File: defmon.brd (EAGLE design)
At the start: 50.8 x 48.1 mm, 18 parts, among them IC2 MEGA8-P, Q1 20MHz, X1 MAB5SH, X2 1503_09

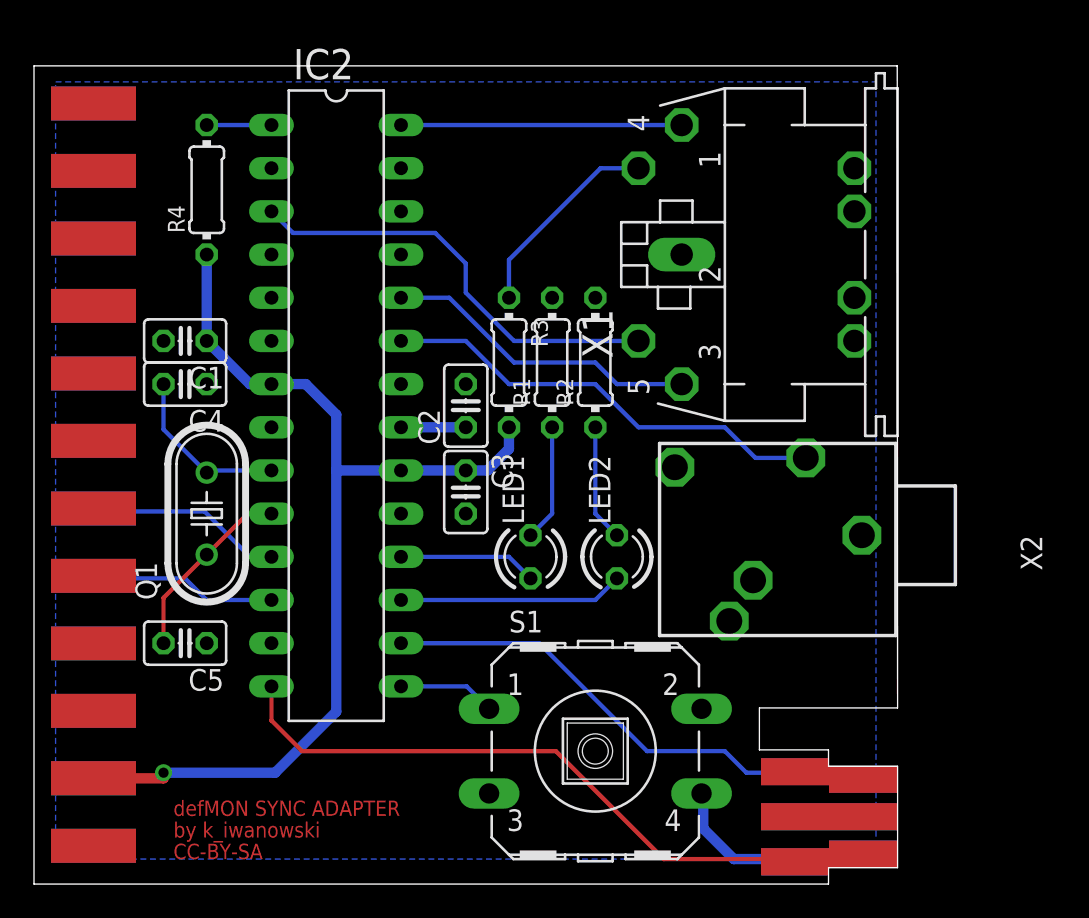
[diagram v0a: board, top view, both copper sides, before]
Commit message: added a new jack socket
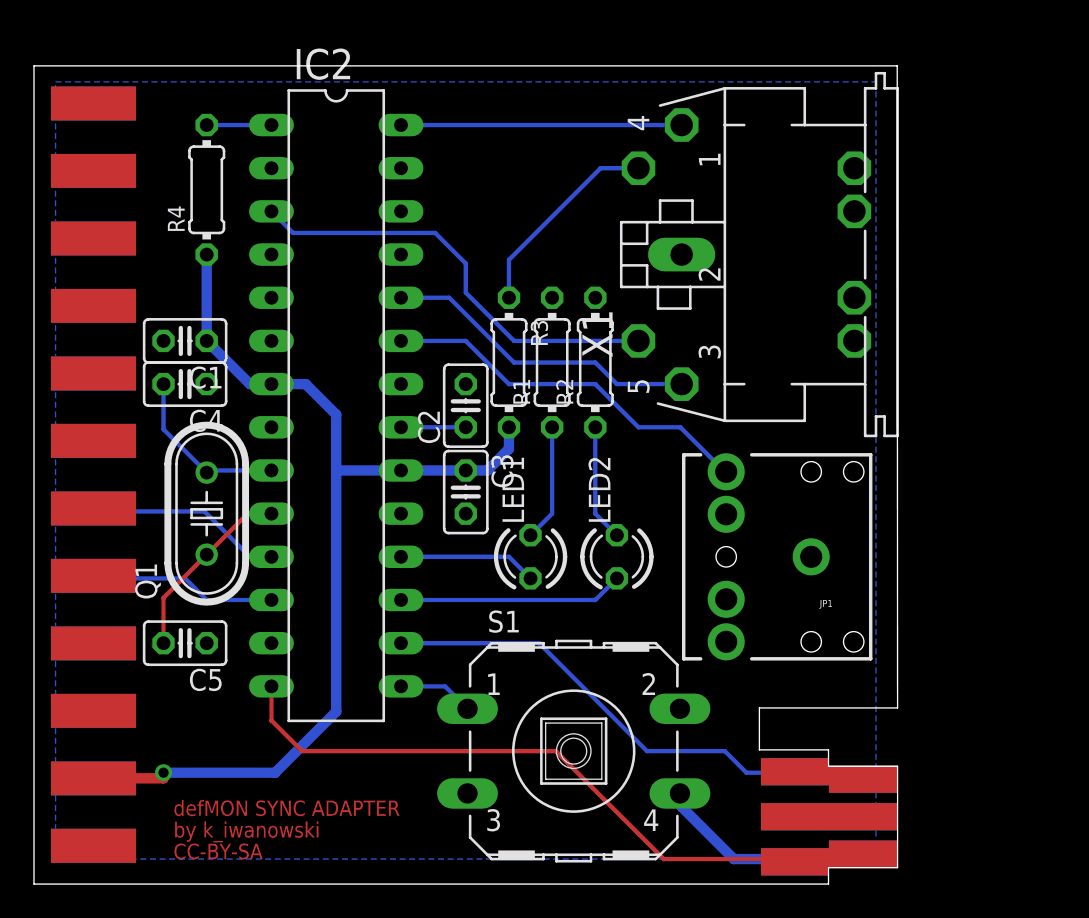
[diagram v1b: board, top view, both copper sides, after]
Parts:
- removed X2: 1503_09, con-lumberg:1503_09
- added JP1: (no value), SparkFun-Connectors:AUDIO-JACK
- moved S1 1.27 mm to (31.8, 7.62)
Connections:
- net GND: now also JP1.SLEEVE; no longer X2.1
- net TRIG1: now also JP1.TIP; no longer X2.2
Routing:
- net TRIG1: track 26.7 -> 22.3 mm
- net N$4: track 5.73 -> 4.46 mm
- net GND: track 12.6 -> 13.1 mm
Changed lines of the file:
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@@
 <layer number="54" name="bGND_GNDA" color="1" fill="9" visible="no" active="no"/>
 <layer number="56" name="wert" color="7" fill="1" visible="no" active="no"/>
+<layer number="57" name="tCAD" color="7" fill="1" visible="no" active="no"/>
+<layer number="90" name="Modules" color="5" fill="1" visible="yes" active="yes"/>
 <layer number="91" name="Nets" color="2" fill="1" visible="no" active="no"/>
 <layer number="92" name="Busses" color="1" fill="1" visible="no" active="no"/>
@@
 <layer number="97" name="Info" color="7" fill="1" visible="no" active="no"/>
 <layer number="98" name="Guide" color="6" fill="1" visible="no" active="no"/>
+<layer number="99" name="SpiceOrder" color="7" fill="1" visible="no" active="no"/>
 <layer number="100" name="Muster" color="7" fill="1" visible="no" active="no"/>
 <layer number="101" name="Patch_Top" color="12" fill="4" visible="no" active="yes"/>
@@
 <layer number="106" name="bPlate" color="7" fill="1" visible="no" active="yes"/>
 <layer number="107" name="Crop" color="7" fill="1" visible="no" active="yes"/>
+<layer number="108" name="tplace-old" color="10" fill="1" visible="yes" active="yes"/>
+<layer number="109" name="ref-old" color="11" fill="1" visible="yes" active="yes"/>
+<layer number="110" name="fp0" color="7" fill="1" visible="yes" active="yes"/>
+<layer number="111" name="LPC17xx" color="7" fill="1" visible="yes" active="yes"/>
+<layer number="112" name="tSilk" color="7" fill="1" visible="yes" active="yes"/>
+<layer number="113" name="IDFDebug" color="4" fill="1" visible="yes" active="yes"/>
 <layer number="116" name="Patch_BOT" color="9" fill="4" visible="no" active="yes"/>
 <layer number="121" name="_tsilk" color="7" fill="1" visible="no" active="yes"/>
 <layer number="122" name="_bsilk" color="7" fill="1" visible="no" active="yes"/>
+<layer number="123" name="tTestmark" color="7" fill="1" visible="yes" active="yes"/>
+<layer number="124" name="bTestmark" color="7" fill="1" visible="yes" active="yes"/>
 <layer number="125" name="_tNames" color="7" fill="1" visible="no" active="yes"/>
+<layer number="126" name="_bNames" color="7" fill="1" visible="yes" active="yes"/>
+<layer number="127" name="_tValues" color="7" fill="1" visible="yes" active="yes"/>
+<layer number="128" name="_bValues" color="7" fill="1" visible="yes" active="yes"/>
+<layer number="131" name="tAdjust" color="7" fill="1" visible="yes" active="yes"/>
+<layer number="132" name="bAdjust" color="7" fill="1" visible="yes" active="yes"/>
 <layer number="144" name="Drill_legend" color="7" fill="1" visible="no" active="yes"/>
+<layer number="150" name="Notes" color="7" fill="1" visible="yes" active="yes"/>
 <layer number="151" name="HeatSink" color="7" fill="1" visible="no" active="yes"/>
+<layer number="152" name="_bDocu" color="7" fill="1" visible="yes" active="yes"/>
+<layer number="153" name="FabDoc1" color="7" fill="1" visible="yes" active="yes"/>
+<layer number="154" name="FabDoc2" color="7" fill="1" visible="yes" active="yes"/>
+<layer number="155" name="FabDoc3" color="7" fill="1" visible="yes" active="yes"/>
 <layer number="199" name="Contour" color="7" fill="1" visible="no" active="yes"/>
 <layer number="200" name="200bmp" color="1" fill="10" visible="no" active="yes"/>
@@
 <layer number="223" name="223bmp" color="24" fill="1" visible="no" active="no"/>
 <layer number="224" name="224bmp" color="25" fill="1" visible="no" active="no"/>
+<layer number="248" name="Housing" color="7" fill="1" visible="yes" active="yes"/>
+<layer number="249" name="Edge" color="7" fill="1" visible="yes" active="yes"/>
 <layer number="250" name="Descript" color="3" fill="1" visible="no" active="no"/>
 <layer number="251" name="SMDround" color="12" fill="11" visible="no" active="no"/>
@@
 <element name="C3" library="rcl" package="C025-025X050" value="100nf" x="25.4" y="22.86" rot="R270"/>
 <element name="LED1" library="led" package="LED3MM" value="" x="29.21" y="19.05" rot="R90"/>
-<element name="S1" library="switch-omron" package="B3F-40XX" value="" x="33.02" y="7.62">
-<attribute name="OC_NEWARK" value="36K3105" x="33.02" y="7.62" size="1.778" layer="27" display="off"/>
-<attribute name="MPN" value="B3F-4000" x="33.02" y="7.62" size="1.778" layer="27" display="off"/>
-<attribute name="MF" value="OMRON COMPONENTS USA" x="33.02" y="7.62" size="1.778" layer="27" display="off"/>
-<attribute name="OC_FARNELL" value="176434" x="33.02" y="7.62" size="1.778" layer="27" display="off"/>
+<element name="S1" library="switch-omron" package="B3F-40XX" value="" x="31.75" y="7.62">
+<attribute name="OC_NEWARK" value="36K3105" x="31.75" y="7.62" size="1.778" layer="27" display="off"/>
+<attribute name="MPN" value="B3F-4000" x="31.75" y="7.62" size="1.778" layer="27" display="off"/>
+<attribute name="MF" value="OMRON COMPONENTS USA" x="31.75" y="7.62" size="1.778" layer="27" display="off"/>
+<attribute name="OC_FARNELL" value="176434" x="31.75" y="7.62" size="1.778" layer="27" display="off"/>
 </element>
 <element name="X1" library="con-hirschmann" package="MAB5SH" value="MAB5SH" x="43.18" y="36.83" rot="R90">
@@
 <element name="LED2" library="led" package="LED3MM" value="" x="34.29" y="19.05" rot="R90"/>
 <element name="R3" library="rcl" package="0204/7" value="220" x="27.94" y="30.48" rot="R270"/>
-<element name="X2" library="con-lumberg" package="1503_09" value="1503_09" x="50.8" y="20.32" rot="R270">
-<attribute name="OC_NEWARK" value="unknown" x="50.8" y="20.32" size="1.778" layer="27" rot="R270" display="off"/>
-<attribute name="MPN" value="" x="50.8" y="20.32" size="1.778" layer="27" rot="R270" display="off"/>
-<attribute name="MF" value="" x="50.8" y="20.32" size="1.778" layer="27" rot="R270" display="off"/>
-<attribute name="OC_FARNELL" value="1243244" x="50.8" y="20.32" size="1.778" layer="27" rot="R270" display="off"/>
-</element>
 <element name="C1" library="rcl" package="C025-025X050" value="100nf" x="8.89" y="31.75" rot="R180"/>
 <element name="C2" library="rcl" package="C025-025X050" value="100nf" x="25.4" y="27.94" rot="R90"/>
@@
 <element name="C5" library="rcl" package="C025-025X050" value="22p" x="8.89" y="13.97" rot="R180"/>
 <element name="R4" library="rcl" package="0204/7" value="10k" x="10.16" y="40.64" rot="R90"/>
+<element name="JP1" library="SparkFun-Connectors" package="AUDIO-JACK" value="" x="45.72" y="19.05" rot="R180"/>
 </elements>
 <signals>
@@
 <contactref element="S1" pad="4"/>
 <contactref element="U$1" pad="6"/>
-<contactref element="X2" pad="1"/>
-<wire x1="39.2684" y1="5.1308" x2="39.37" y2="5.1308" width="0.6096" layer="16"/>
-<wire x1="39.37" y1="5.1308" x2="39.37" y2="3.06605" width="0.6096" layer="16"/>
-<wire x1="39.37" y1="3.06605" x2="41.16605" y2="1.27" width="0.6096" layer="16"/>
+<wire x1="37.9984" y1="5.1308" x2="38.1" y2="5.1308" width="0.6096" layer="16"/>
+<wire x1="38.1" y1="5.1308" x2="38.1" y2="4.33605" width="0.6096" layer="16"/>
+<wire x1="38.1" y1="4.33605" x2="41.16605" y2="1.27" width="0.6096" layer="16"/>
 <wire x1="41.16605" y1="1.27" x2="48.768" y2="1.27" width="0.6096" layer="16"/>
 <wire x1="48.768" y1="1.27" x2="48.768" y2="1.562" width="0.6096" layer="16"/>
@@
 <contactref element="C5" pad="1"/>
 <contactref element="C1" pad="2"/>
+<contactref element="JP1" pad="SLEEVE"/>
 </signal>
 <signal name="PE">
@@
 <contactref element="S1" pad="1"/>
 <contactref element="IC2" pad="15"/>
-<wire x1="21.59" y1="11.43" x2="25.4508" y2="11.43" width="0.254" layer="16"/>
-<wire x1="25.4508" y1="11.43" x2="26.7716" y2="10.1092" width="0.254" layer="16"/>
+<wire x1="21.59" y1="11.43" x2="24.1808" y2="11.43" width="0.254" layer="16"/>
+<wire x1="24.1808" y1="11.43" x2="25.5016" y2="10.1092" width="0.254" layer="16"/>
 </signal>
 <signal name="N$5">
@@
 <signal name="TRIG1">
 <contactref element="IC2" pad="23"/>
-<contactref element="X2" pad="2"/>
-<wire x1="45.4" y1="24.87" x2="42.44" y2="24.87" width="0.254" layer="16"/>
-<wire x1="42.44" y1="24.87" x2="40.64" y2="26.67" width="0.254" layer="16"/>
-<wire x1="40.64" y1="26.67" x2="35.56" y2="26.67" width="0.254" layer="16"/>
+<wire x1="40.64" y1="24.05" x2="38.02" y2="26.67" width="0.254" layer="16"/>
+<wire x1="38.02" y1="26.67" x2="35.56" y2="26.67" width="0.254" layer="16"/>
 <wire x1="35.56" y1="26.67" x2="33.02" y2="29.21" width="0.254" layer="16"/>
 <wire x1="33.02" y1="29.21" x2="27.94" y2="29.21" width="0.254" layer="16"/>
 <wire x1="27.94" y1="29.21" x2="25.4" y2="31.75" width="0.254" layer="16"/>
 <wire x1="25.4" y1="31.75" x2="21.59" y2="31.75" width="0.254" layer="16"/>
+<contactref element="JP1" pad="TIP"/>
+<wire x1="40.72" y1="24.05" x2="40.64" y2="24.05" width="0.254" layer="16"/>
 </signal>
 <signal name="TRIG2">
@@
 <contactref element="C2" pad="1"/>
 <contactref element="IC2" pad="21"/>
-<wire x1="21.59" y1="26.67" x2="25.4" y2="26.67" width="0.6096" layer="16"/>
+<wire x1="21.59" y1="26.67" x2="25.4" y2="26.67" width="0.254" layer="16"/>
 </signal>
 <signal name="N$8">
